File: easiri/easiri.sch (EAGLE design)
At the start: 44 parts

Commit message: usartとかを追加
電源確認or通信確認ようledをついか、pcでシリアルモニタによるデバッグができるようにusartを追加
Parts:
- removed BOX10P-L1: BOX10P, user_conector:BOX10P
- added R_I5: 1k, user_rcl:R_SHUGOU
- added U$22: BOX14P, user_conector:BOX14P
- added U$23: RGB_LED, user_leds:RGB_LED
- U$12: value XT60 -> YUROBLOCK2; device user_conector:XT60 -> user_conector:YUROBLOCK2
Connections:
- new net N$11: R_I5.8, U$1.PIN27
- new net N$40: R_I5.7, U$1.PIN28
- new net N$42: R_I5.4, U$23.B_A
- new net N$43: R_I5.1, U$23.R_A
- new net N$44: R_I5.2, U$23.G_A
- new net RX: U$1.PIN30, U$22.P$13
- new net TX: U$1.PIN29, U$22.P$14
- net GND: now also U$22.P$11, U$22.P$5, U$22.P$7, U$23.B_K, U$23.G_K, U$23.R_K; no longer BOX10P-L1.P$3, BOX10P-L1.P$5, BOX10P-L1.P$9
- net GNDA: now also U$12.P$1; no longer U$12.-
- net JTCK: now also U$22.P$6; no longer BOX10P-L1.P$4
- net JTDI: now also U$22.P$10; no longer BOX10P-L1.P$8
- net JTDO: now also U$22.P$8; no longer BOX10P-L1.P$6
- net JTMS: now also U$22.P$4; no longer BOX10P-L1.P$2
- net NRST: now also U$22.P$12; no longer BOX10P-L1.P$10
- net V3.3: now also R_I5.5, U$22.P$3; no longer BOX10P-L1.P$1
- net VDD: now also U$12.P$2; no longer U$12.+
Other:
- moved on the sheet: R3

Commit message: canトランシーバ用のコンデンサを追加
fet駆動にインバッタをはっさんだ。ゲートにledを入れたがそれがそのままプルダウン抵抗に置き換わるかも
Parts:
- removed U$13, U$14, U$15, U$16, U$17, U$18, U$19, U$20: XH_2P, user_conector:XH_2P
- added C12, C13, C14: 0.1u, rcl:C-EUC1608
- added ES1, ES2, ES3, ES4, ES5, ES6, ES7, ES8: XH_2P, user_conector:XH_2P
- added LED1: 抵抗内蔵led, led:LED5MM
- added LED2, LED3, LED4, LED5, LED6, LED7, LED8, LED9: (no value), user_leds:1608LED
- added NAND1, NAND2: (no value), user_ic:14PIN_NAND2
- added R_I6, R_I7: (no value), user_rcl:R_SHUGOU2
- R_I3, R_I4: value (none) -> 10k
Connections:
- new net N$45: NAND1.2Y, R_I6.3, U$11.PIN1_G1
- new net N$46: ES5.P$2, U$10.PIN4_D2
- new net N$47: NAND2.3A, NAND2.3B, R_I3.2, U$6.2_C
- new net N$48: NAND2.1A, NAND2.1B, R_I3.4, U$6.4_C
- new net N$49: NAND1.4A, NAND1.4B, R_I4.1, U$7.1_C
- new net N$50: NAND1.3Y, R_I6.8, U$10.PIN1_G1
- new net N$51: NAND2.1Y, R_I7.2, U$9.PIN3_G2
- new net N$52: NAND2.2Y, R_I7.3, U$9.PIN1_G1
- new net N$53: NAND2.3Y, R_I7.8, U$8.PIN1_G1
- new net N$54: NAND2.4Y, R_I7.5, U$8.PIN3_G2
- new net N$55: LED9.A, R_I6.4
- new net N$56: LED6.A, R_I6.1
- new net N$57: NAND1.4Y, R_I6.5, U$10.PIN3_G2
- new net N$58: LED3.A, R_I7.7
- new net N$59: LED5.A, R_I7.4
- new net N$60: LED2.A, R_I7.1
- net GND: now also C14.2
- net GNDA: now also C12.2, C13.2, LED1.C, LED2.K, LED3.K, LED4.K, LED5.K, LED6.K, LED7.K, LED8.K, LED9.K, NAND1.GND, NAND2.GND
- net N$13: now also NAND2.4A, NAND2.4B; no longer U$8.PIN1_G1
- net N$17: now also NAND1.2A, NAND1.2B, R_I4.3, U$7.3_C; no longer R_I3.2, U$6.2_C, U$8.PIN3_G2
- net N$18: now also NAND2.2A, NAND2.2B; no longer U$9.PIN1_G1
- net N$19: now also NAND1.1A, NAND1.1B, R_I4.4, U$7.4_C; no longer R_I3.4, U$6.4_C, U$9.PIN3_G2
- net N$20: now also NAND1.1Y, R_I6.2, U$11.PIN3_G2; no longer R_I4.1, U$10.PIN1_G1, U$7.1_C
- net N$21: now also NAND1.3A, NAND1.3B; no longer U$10.PIN3_G2
- net N$22: now also LED8.A, R_I6.6; no longer R_I4.3, U$11.PIN1_G1, U$7.3_C
- net N$23: now also LED7.A, R_I6.7; no longer R_I4.4, U$11.PIN3_G2, U$7.4_C
- net N$24: now also ES3.P$2; no longer U$15.P$2
- net N$25: now also ES1.P$2, U$8.PIN4_D2; no longer U$13.P$2, U$8.PIN6_D1
- net N$26: now also ES2.P$2, U$8.PIN6_D1; no longer U$14.P$2, U$8.PIN4_D2
- net N$27: now also ES4.P$2; no longer U$16.P$2
- net N$28: now also LED4.A, R_I7.6; no longer U$10.PIN6_D1, U$17.P$2
- net N$29: now also ES6.P$2, U$10.PIN6_D1; no longer U$10.PIN4_D2, U$18.P$2
- net N$30: now also ES7.P$2; no longer U$19.P$2
- net N$32: now also ES8.P$2; no longer U$20.P$2
- net VCC: now also C14.1
- net VDD: now also C12.1, C13.1, ES1.P$1, ES2.P$1, ES3.P$1, ES4.P$1, ES5.P$1, ES6.P$1, ES7.P$1, ES8.P$1, LED1.A, NAND1.VCC, NAND2.VCC; no longer U$13.P$1, U$14.P$1, U$15.P$1, U$16.P$1, U$17.P$1, U$18.P$1, U$19.P$1, U$20.P$1

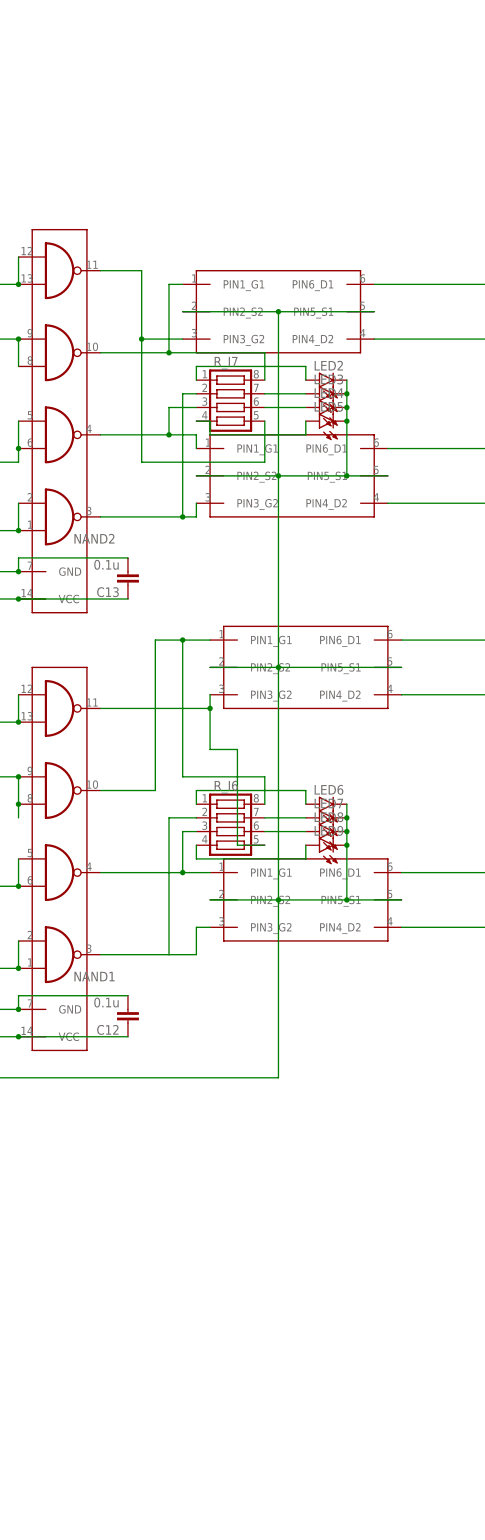
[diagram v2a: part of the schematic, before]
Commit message: ゲートにプルダウン抵抗を追加
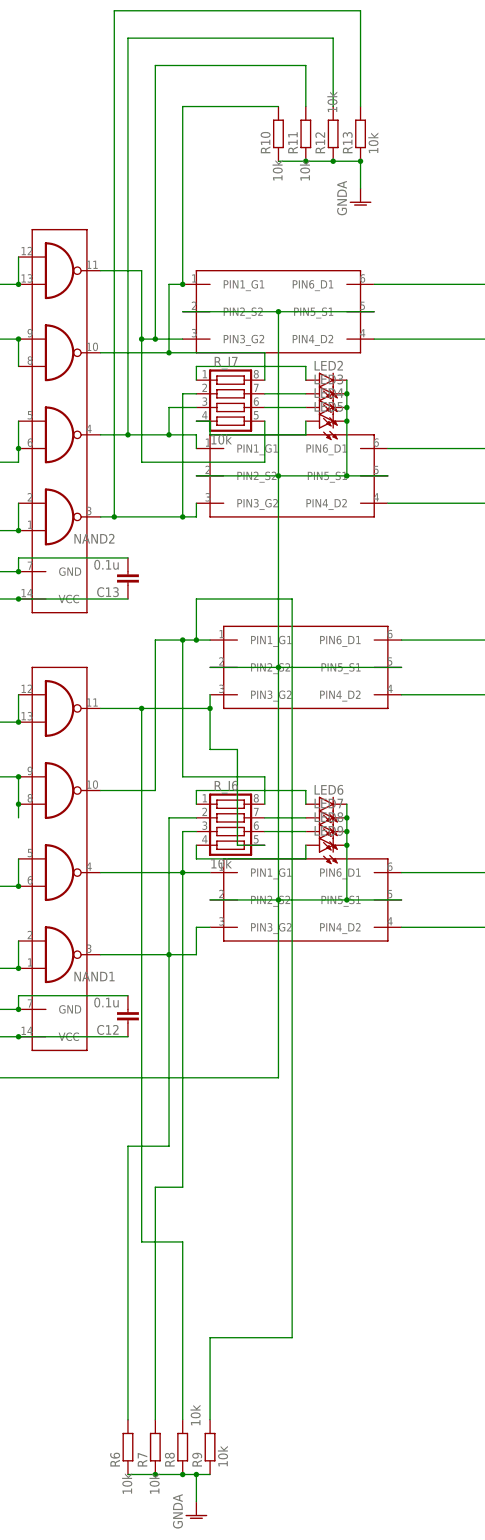
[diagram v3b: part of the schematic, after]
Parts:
- added R10, R11, R12, R13, R6, R7, R8, R9: 10k, user_rcl:R_REG
- R_I6, R_I7: value (none) -> 10k
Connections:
- net GNDA: now also R10.1, R11.1, R12.1, R13.1, R6.1, R7.1, R8.1, R9.1
- net N$20: now also R6.2
- net N$45: now also R7.2
- net N$50: now also R9.2
- net N$51: now also R13.2
- net N$52: now also R12.2
- net N$53: now also R10.2
- net N$54: now also R11.2
- net N$57: now also R8.2

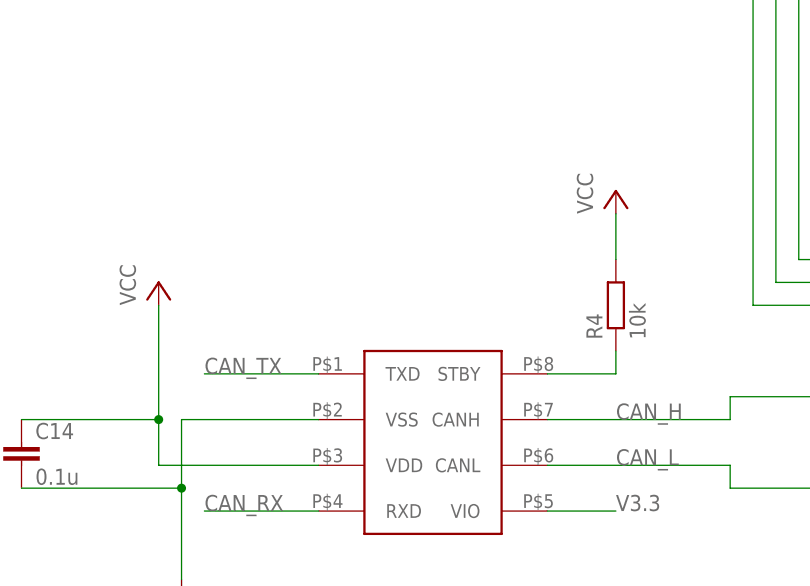
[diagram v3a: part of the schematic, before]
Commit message: mcp2562スタンバイピンプルダウン
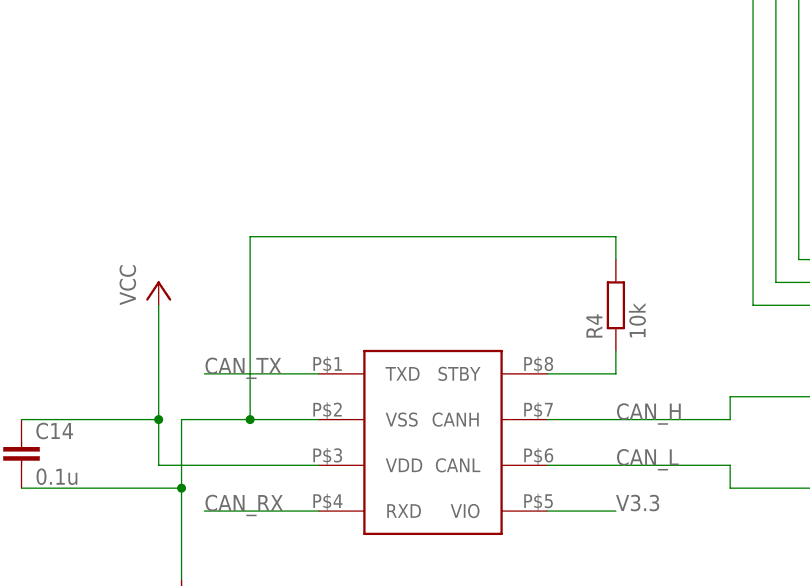
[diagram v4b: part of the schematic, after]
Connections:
- net GND: now also R4.2
- net VCC: no longer R4.2
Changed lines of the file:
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@@
 <part name="P+3" library="supply1" library_urn="urn:adsk.eagle:library:371" deviceset="VCC" device=""/>
 <part name="R4" library="user_rcl" deviceset="R_REG" device="" value="10k"/>
-<part name="P+4" library="supply1" library_urn="urn:adsk.eagle:library:371" deviceset="VCC" device=""/>
 <part name="R5" library="user_rcl" deviceset="R_REG" device="" value="120"/>
 <part name="U$6" library="user_ic" deviceset="TLP290-4" device=""/>
@@
 <attribute name="VALUE" x="214.122" y="26.67" size="1.778" layer="96" rot="R90"/>
 </instance>
-<instance part="P+4" gate="VCC" x="210.82" y="43.18" smashed="yes">
-<attribute name="VALUE" x="208.28" y="40.64" size="1.778" layer="96" rot="R90"/>
-</instance>
 <instance part="R5" gate="G$1" x="236.22" y="15.24" smashed="yes" rot="R90">
 <attribute name="NAME" x="234.7214" y="11.43" size="1.778" layer="95" rot="R90"/>
@@
 <segment>
 <pinref part="U$5" gate="G$1" pin="VSS"/>
-<wire x1="177.8" y1="17.78" x2="162.56" y2="17.78" width="0.1524" layer="91"/>
+<wire x1="177.8" y1="17.78" x2="170.18" y2="17.78" width="0.1524" layer="91"/>
+<wire x1="170.18" y1="17.78" x2="162.56" y2="17.78" width="0.1524" layer="91"/>
 <wire x1="162.56" y1="17.78" x2="162.56" y2="10.16" width="0.1524" layer="91"/>
 <pinref part="GND9" gate="1" pin="GND"/>
@@
 <wire x1="144.78" y1="10.16" x2="162.56" y2="10.16" width="0.1524" layer="91"/>
 <junction x="162.56" y="10.16"/>
+<pinref part="R4" gate="G$1" pin="2"/>
+<wire x1="210.82" y1="35.56" x2="210.82" y2="38.1" width="0.1524" layer="91"/>
+<wire x1="210.82" y1="38.1" x2="170.18" y2="38.1" width="0.1524" layer="91"/>
+<wire x1="170.18" y1="38.1" x2="170.18" y2="17.78" width="0.1524" layer="91"/>
+<junction x="170.18" y="17.78"/>
 </segment>
 <segment>
@@
 <junction x="160.02" y="17.78"/>
 </segment>
-<segment>
-<pinref part="P+4" gate="VCC" pin="VCC"/>
-<pinref part="R4" gate="G$1" pin="2"/>
-<wire x1="210.82" y1="40.64" x2="210.82" y2="35.56" width="0.1524" layer="91"/>
-</segment>
 </net>
